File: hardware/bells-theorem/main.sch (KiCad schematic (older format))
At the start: 4 parts, among them J2 left, J3 right, U1 Teensy4.1

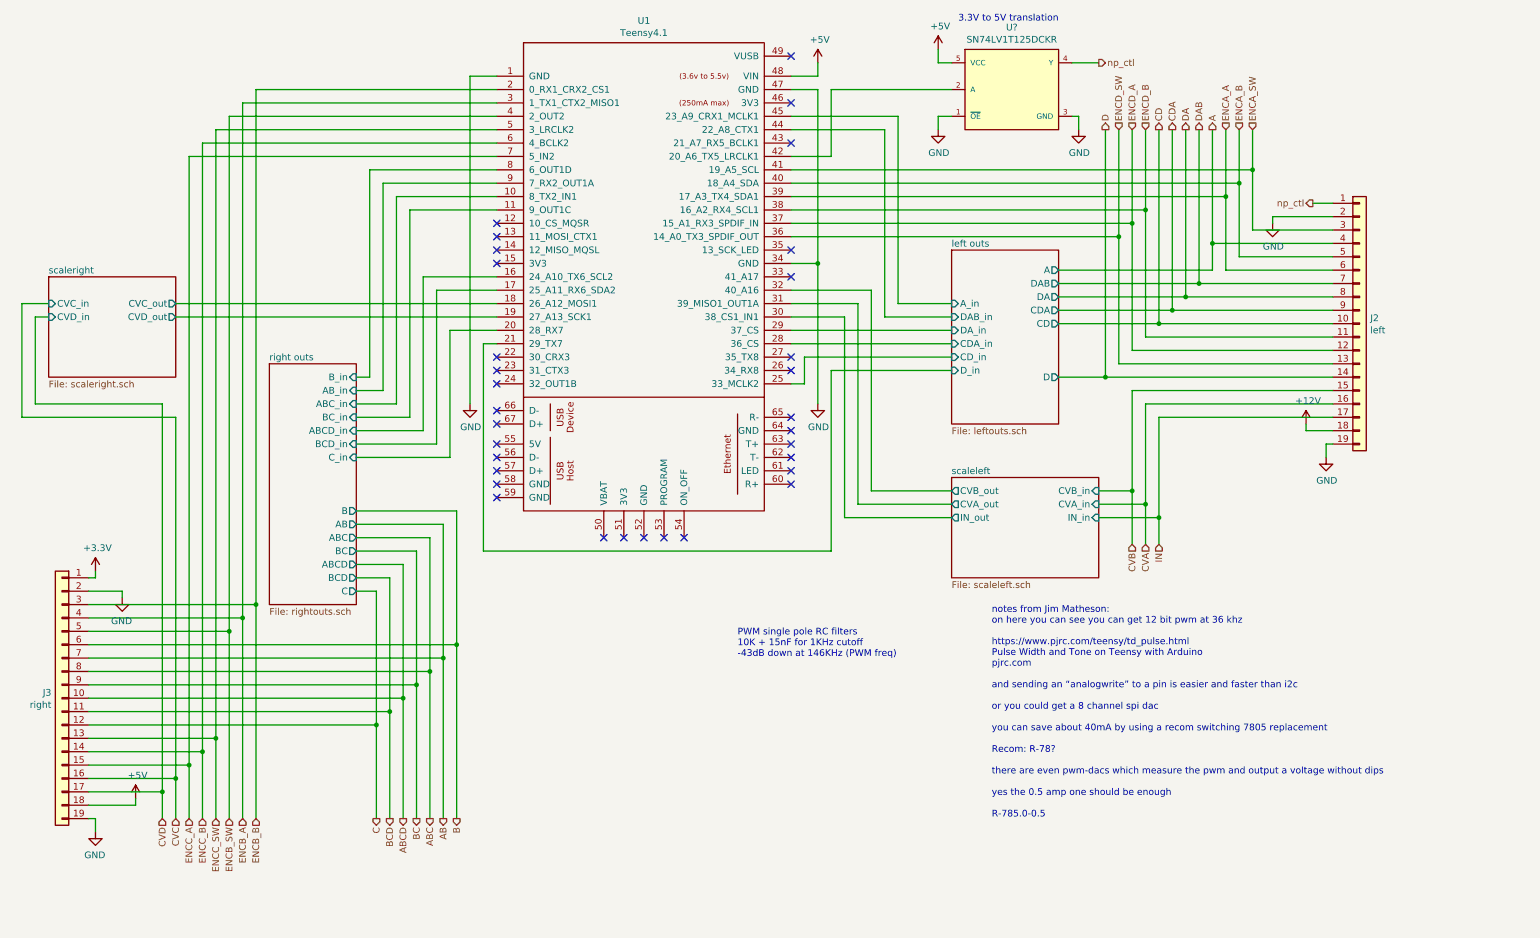
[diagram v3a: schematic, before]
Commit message: modified for Kicad 6 updated testing code
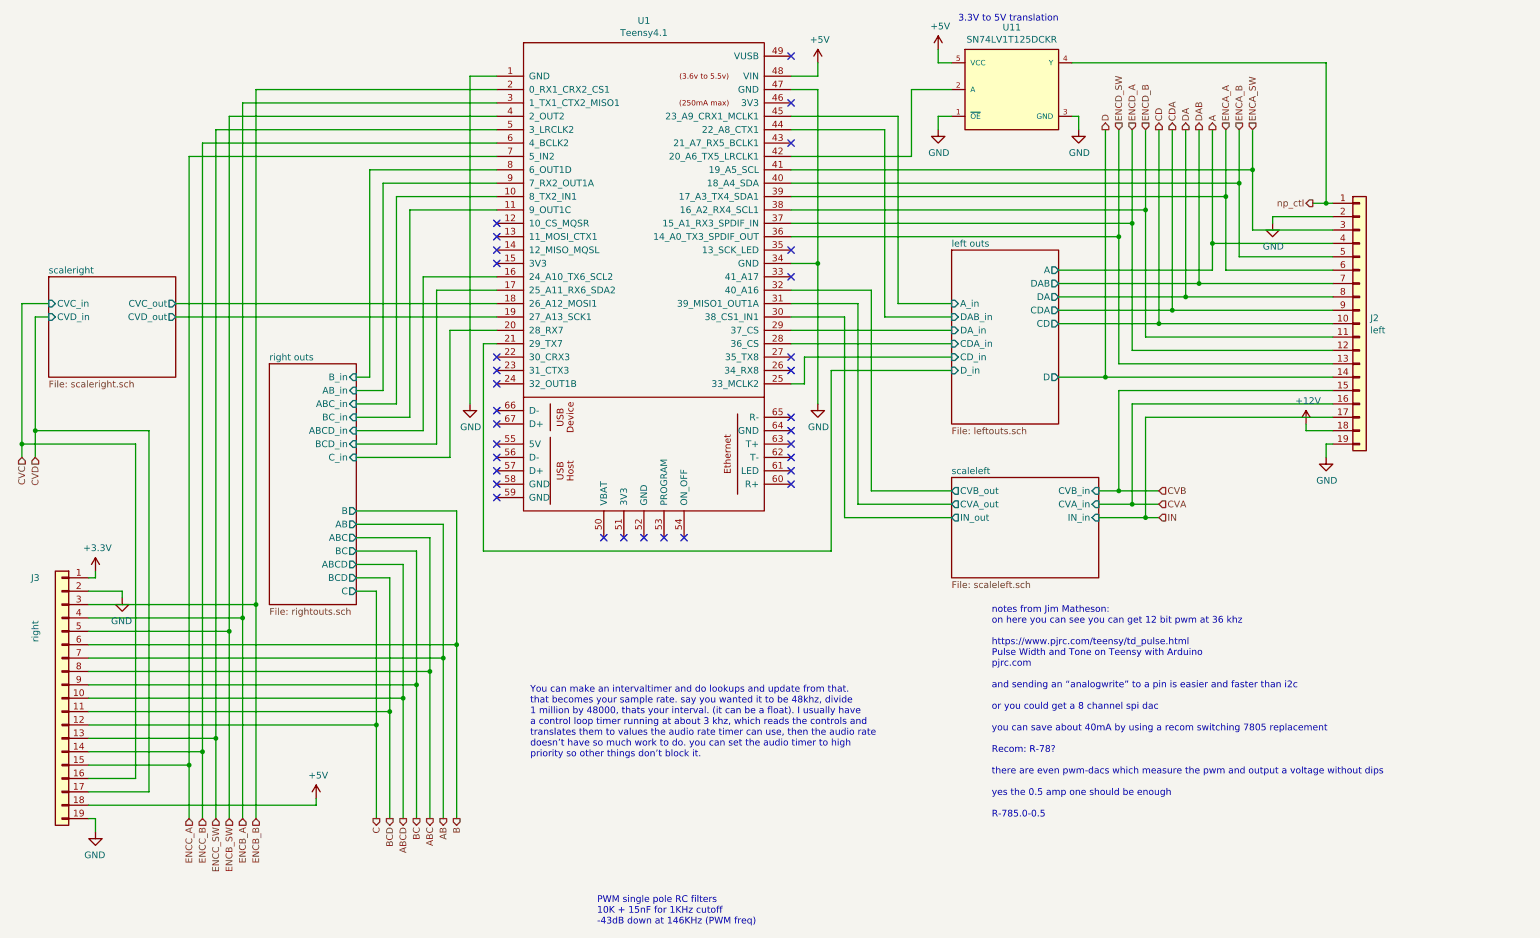
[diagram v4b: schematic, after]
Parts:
- J2, J3: footprint Connector_PinSocket_2.54mm:PinSocket_1x19_P2.54mm_Vertical -> (none)
- gave numbers to parts that had none: 1
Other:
- note added: "You can make an intervaltimer and do lookups and update from that. \nthat becomes your sample rate. say you wanted it to be 48khz, divide \n1 million by 48000, thats your interval. (it can be a float). I usually have \na control loop timer running at about 3 khz, which reads the controls and\ntranslates them to values the audio rate timer can use, then the audio rate\ndoesn’t have so much work to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"
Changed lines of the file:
@@
 	1900 2700 4300 2700
-Wire Wire Line
-	3400 5850 1250 5850
 Wire Wire Line
 	3500 5750 1250 5750
@@
 Wire Wire Line
 	2400 1200 2400 5050
-Connection ~ 1900 6250
-Wire Wire Line
-	1900 3550 1900 6250
-Wire Wire Line
-	750  3550 1900 3550
-Wire Wire Line
-	750  2700 750  3550
+Wire Wire Line
+	750  2700 750  3750
 Wire Wire Line
 	950  2700 750  2700
-Connection ~ 1800 6350
-Wire Wire Line
-	1800 3450 1800 6350
-Wire Wire Line
-	850  3450 1800 3450
-Wire Wire Line
-	850  2800 850  3450
+Wire Wire Line
+	850  2800 850  3650
 Wire Wire Line
 	950  2800 850  2800
@@
 	1    0    0    -1
 $EndComp
-Text Notes 6100 5350 0    50   ~ 0
+Text Notes 5050 7350 0    50   ~ 0
 PWM single pole RC filters\n10K + 15nF for 1KHz cutoff\n-43dB down at 146KHz (PWM freq)
 Text Notes 8000 6550 0    50   ~ 0
 notes from Jim Matheson:\non here you can see you can get 12 bit pwm at 36 khz\n\nhttps://www.pjrc.com/teensy/td_pulse.html\nPulse Width and Tone on Teensy with Arduino\npjrc.com\n\nand sending an “analogwrite” to a pin is easier and faster than i2c\n\nor you could get a 8 channel spi dac\n\nyou can save about 40mA by using a recom switching 7805 replacement\n\nRecom: R-78?\n\nthere are even pwm-dacs which measure the pwm and output a voltage without dips\n\nyes the 0.5 amp one should be enough\n\nR-785.0-0.5\n
-Connection ~ 9150 4200
-Wire Wire Line
-	9150 3450 9150 4200
-Wire Wire Line
-	10550 3450 9150 3450
-Connection ~ 9050 4100
-Wire Wire Line
-	9050 3350 9050 4100
-Wire Wire Line
-	10550 3350 9050 3350
-Wire Wire Line
-	9050 4100 9050 4500
-Wire Wire Line
-	8800 4100 9050 4100
-Wire Wire Line
-	9150 4200 9150 4500
-Wire Wire Line
-	8800 4200 9150 4200
-Wire Wire Line
-	9250 4300 9250 4500
-Connection ~ 9250 4300
-Wire Wire Line
-	8800 4300 9250 4300
+Wire Wire Line
+	8800 4100 8950 4100
+Wire Wire Line
+	8800 4200 9050 4200
+Wire Wire Line
+	8800 4300 9150 4300
 $Sheet
 S 7700 4000 1100 750
@@
 F5 "CVD_in" I L 950 2800 50
 $EndSheet
-Wire Wire Line
-	9250 3550 9250 4300
 Text HLabel 3600 6550 3    50   Output ~ 0
 ABCD
 Text HLabel 3700 6550 3    50   Output ~ 0
 BC
-Wire Wire Line
-	9250 3550 10550 3550
 Wire Wire Line
 	1250 5050 2400 5050
@@
 Text HLabel 2400 6550 3    50   Input ~ 0
 ENCB_A
-Text HLabel 1800 6550 3    50   Input ~ 0
+Text HLabel 850  3850 3    50   Input ~ 0
 CVD
-Text HLabel 1900 6550 3    50   Input ~ 0
+Text HLabel 750  3850 3    50   Input ~ 0
 CVC
 Text HLabel 2200 6550 3    50   Input ~ 0
@@
 Wire Wire Line
 	2000 6150 2000 6550
-Wire Wire Line
-	1900 6250 1900 6550
-Wire Wire Line
-	1800 6350 1800 6550
-Wire Wire Line
-	1250 6350 1800 6350
 Text HLabel 3400 6550 3    50   Output ~ 0
 C
-Wire Wire Line
-	1250 6250 1900 6250
 Wire Wire Line
 	1250 6150 2000 6150
@@
 	1300 6650 1300 6550
 Wire Wire Line
-	1600 6450 1250 6450
-Wire Wire Line
-	1600 6400 1600 6450
+	2950 6400 2950 6450
 Wire Wire Line
 	1500 4850 1250 4850
@@
 F 3 "" H 10100 2100 50  0001 C CNN
 	1    10100 2100
-	1    0    0    -1
-$EndComp
-$Comp
-L Connectors_Generic:Conn_01x19 J3
-U 1 1 5F85F4C1
-P 1050 5650
-F 0 "J3" H 1130 5692 50  0000 L CNN
-F 1 "right" H 1130 5601 50  0000 L CNN
-F 2 "Connector_PinSocket_2.54mm:PinSocket_1x19_P2.54mm_Vertical" H 1050 5650 50  0001 C CNN
-F 3 "~" H 1050 5650 50  0001 C CNN
-	1    1050 5650
-	-1   0    0    -1
-$EndComp
-$Comp
-L Connectors_Generic:Conn_01x19 J2
-U 1 1 5F85C3F5
-P 10750 2850
-F 0 "J2" H 10830 2892 50  0000 L CNN
-F 1 "left" H 10830 2801 50  0000 L CNN
-F 2 "Connector_PinSocket_2.54mm:PinSocket_1x19_P2.54mm_Vertical" H 10750 2850 50  0001 C CNN
-F 3 "~" H 10750 2850 50  0001 C CNN
-	1    10750 2850
 	1    0    0    -1
 $EndComp
@@
 Text HLabel 4000 6550 3    50   Output ~ 0
 B
-Text HLabel 9050 4500 3    50   Input ~ 0
+Text HLabel 9250 4100 2    50   Input ~ 0
 CVB
-Text HLabel 9150 4500 3    50   Input ~ 0
+Text HLabel 9250 4200 2    50   Input ~ 0
 CVA
-Text HLabel 9250 4500 3    50   Input ~ 0
+Text HLabel 9250 4300 2    50   Input ~ 0
 IN
 Text HLabel 8950 1400 1    50   Input ~ 0
@@
 L power:+5V #PWR039
 U 1 1 60788A4D
-P 1600 6400
-F 0 "#PWR039" H 1600 6250 50  0001 C CNN
-F 1 "+5V" H 1615 6573 50  0000 C CNN
-F 2 "" H 1600 6400 50  0001 C CNN
-F 3 "" H 1600 6400 50  0001 C CNN
-	1    1600 6400
+P 2950 6400
+F 0 "#PWR039" H 2950 6250 50  0001 C CNN
+F 1 "+5V" H 2965 6573 50  0000 C CNN
+F 2 "" H 2950 6400 50  0001 C CNN
+F 3 "" H 2950 6400 50  0001 C CNN
+	1    2950 6400
 	1    0    0    -1
 $EndComp
@@
 np_ctl
 Wire Wire Line
-	10400 1950 10550 1950
-$Comp
-L EEC_lib:SN74LV1T125DCKR U?
+	10400 1950 10500 1950
+$Comp
+L EEC_lib:SN74LV1T125DCKR U11
 U 1 1 615887AF
 P 7700 900
-F 0 "U?" H 8150 1165 50  0000 C CNN
+F 0 "U11" H 8150 1165 50  0000 C CNN
 F 1 "SN74LV1T125DCKR" H 8150 1074 50  0000 C CNN
 F 2 "Texas_Instruments-DCK0005A-0-0-*" H 7700 1300 50  0001 L CNN
@@
 	1    0    0    -1
 $EndComp
-Text HLabel 8800 900  2    50   Output ~ 0
-np_ctl
 Wire Wire Line
 	7100 4100 7700 4100
@@
 P 8650 1400
 AR Path="/5F7954A8/616AED7E" Ref="#PWR?"  Part="1"
-AR Path="/5CEF66AD/616AED7E" Ref="#PWR?"  Part="1"
-F 0 "#PWR?" H 8650 1150 50  0001 C CNN
+AR Path="/5CEF66AD/616AED7E" Ref="#PWR056"  Part="1"
+F 0 "#PWR056" H 8650 1150 50  0001 C CNN
 F 1 "GND" H 8655 1227 50  0000 C CNN
 F 2 "" H 8650 1400 50  0001 C CNN
@@
 P 7600 800
 AR Path="/5F7954A8/616AF3B1" Ref="#PWR?"  Part="1"
-AR Path="/5CEF66AD/616AF3B1" Ref="#PWR?"  Part="1"
-F 0 "#PWR?" H 7600 650 50  0001 C CNN
+AR Path="/5CEF66AD/616AF3B1" Ref="#PWR053"  Part="1"
+F 0 "#PWR053" H 7600 650 50  0001 C CNN
 F 1 "+5V" H 7615 973 50  0000 C CNN
 F 2 "" H 7600 800 50  0001 C CNN
@@
 P 7600 1400
 AR Path="/5F7954A8/616CDDCF" Ref="#PWR?"  Part="1"
-AR Path="/5CEF66AD/616CDDCF" Ref="#PWR?"  Part="1"
-F 0 "#PWR?" H 7600 1150 50  0001 C CNN
+AR Path="/5CEF66AD/616CDDCF" Ref="#PWR054"  Part="1"
+F 0 "#PWR054" H 7600 1150 50  0001 C CNN
 F 1 "GND" H 7605 1227 50  0000 C CNN
 F 2 "" H 7600 1400 50  0001 C CNN
@@
 $EndComp
 Wire Wire Line
-	6500 1600 6800 1600
-Wire Wire Line
-	6800 1600 6800 1100
-Wire Wire Line
-	6800 1100 7700 1100
-Wire Wire Line
-	8600 900  8800 900
+	6500 1600 7400 1600
+Wire Wire Line
+	7400 1600 7400 1100
+Wire Wire Line
+	7400 1100 7700 1100
 Text Notes 7750 600  0    50   ~ 0
 3.3V to 5V translation
+Wire Wire Line
+	1250 6450 2950 6450
+$Comp
+L Connectors_Generic:Conn_01x19 J2
+U 1 1 61639564
+P 10750 2850
+F 0 "J2" H 10830 2892 50  0000 L CNN
+F 1 "left" H 10830 2801 50  0000 L CNN
+F 2 "" H 10750 2850 50  0001 C CNN
+F 3 "~" H 10750 2850 50  0001 C CNN
+	1    10750 2850
+	1    0    0    -1
+$EndComp
+Wire Wire Line
+	10550 3550 9150 3550
+Wire Wire Line
+	9150 3550 9150 4300
+Connection ~ 9150 4300
+Wire Wire Line
+	9150 4300 9250 4300
+Wire Wire Line
+	10550 3450 9050 3450
+Wire Wire Line
+	9050 3450 9050 4200
+Connection ~ 9050 4200
+Wire Wire Line
+	9050 4200 9250 4200
+Wire Wire Line
+	10550 3350 8950 3350
+Wire Wire Line
+	8950 3350 8950 4100
+Connection ~ 8950 4100
+Wire Wire Line
+	8950 4100 9250 4100
+$Comp
+L Connectors_Generic:Conn_01x19 J3
+U 1 1 6167EDD0
+P 1050 5650
+F 0 "J3" H 1250 6550 50  0000 C CNN
+F 1 "right" V 1250 6150 50  0000 C CNN
+F 2 "" H 1050 5650 50  0001 C CNN
+F 3 "~" H 1050 5650 50  0001 C CNN
+	1    1050 5650
+	-1   0    0    -1
+$EndComp
+Wire Wire Line
+	1250 6250 1600 6250
+Wire Wire Line
+	1600 6250 1600 3750
+Wire Wire Line
+	1600 3750 750  3750
+Connection ~ 750  3750
+Wire Wire Line
+	750  3750 750  3850
+Wire Wire Line
+	3400 5850 1250 5850
+Wire Wire Line
+	1250 6350 1700 6350
+Wire Wire Line
+	1700 6350 1700 3650
+Wire Wire Line
+	1700 3650 850  3650
+Connection ~ 850  3650
+Wire Wire Line
+	850  3650 850  3850
+Wire Wire Line
+	10500 900  10500 1950
+Wire Wire Line
+	8600 900  10500 900
+Connection ~ 10500 1950
+Wire Wire Line
+	10500 1950 10550 1950
+Text Notes 4550 6100 0    50   ~ 0
+You can make an intervaltimer and do lookups and update from that. \nthat becomes your sample rate. say you wanted it to be 48khz, divide \n1 million by 48000, thats your interval. (it can be a float). I usually have \na control loop timer running at about 3 khz, which reads the controls and\ntranslates them to values the audio rate timer can use, then the audio rate\ndoesn’t have so much work to do. you can set the audio timer to high \npriority so other things don’t block it.
 $EndSCHEMATC
